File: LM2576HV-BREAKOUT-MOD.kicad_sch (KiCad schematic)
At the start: 16 parts, among them J1 Conn_01x01, J2 Conn_01x01, J3 Conn_01x01, J4 Conn_01x01, U1 LM2576HVS-ADJ

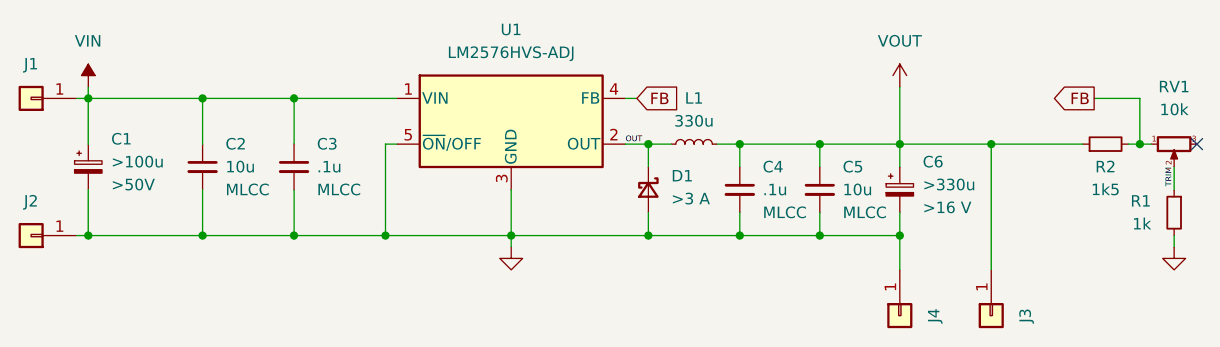
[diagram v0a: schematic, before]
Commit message: Update LM2576HV Breakout Mod to use LM2576HVS-12
- Removed unused potentiometer symbol and associated properties from schematic.
- Updated LM2576HVS-ADJ references to LM2576HVS-12 in schematic, including properties and symbols.
- Adjusted junction and wire positions for better layout.
- Removed redundant wires and no-connects to clean up the schematic.
- Updated connector positions for better alignment.
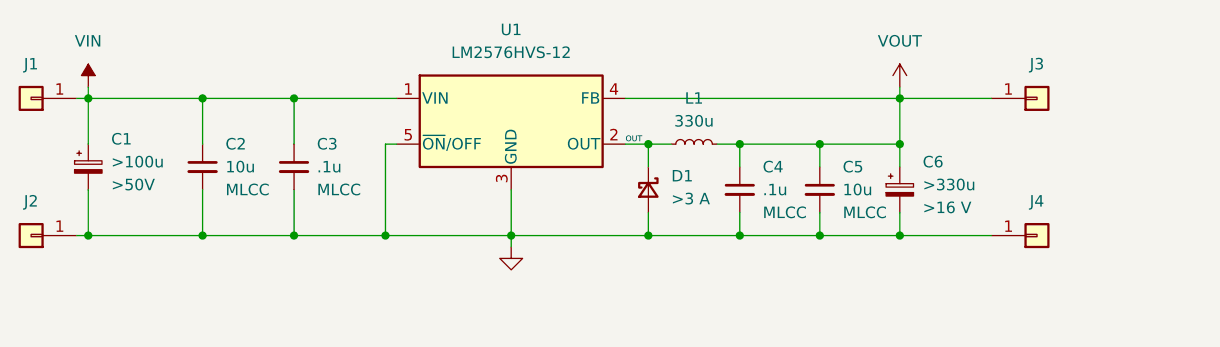
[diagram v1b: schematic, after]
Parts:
- removed R1: 1k, Resistor_SMD:R_0805_2012Metric, symbol Device:R_Small
- removed R2: 1k5, Resistor_SMD:R_0805_2012Metric, symbol Device:R_Small
- removed RV1: 10k, Potentiometer_THT:Potentiometer_Bourns_3296W_Vertical, symbol Device:R_Potentiometer_Small
- removed U1: LM2576HVS-ADJ, Package_TO_SOT_SMD:TO-263-5_TabPin3, symbol Regulator_Switching:LM2576HVS-ADJ
- added U1: LM2576HVS-12, Package_TO_SOT_SMD:TO-263-5_TabPin3, symbol Regulator_Switching:LM2576HVS-12
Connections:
- net GND: now also U1.3 (GND), U1.5 (~{ON}/OFF)
- net OUT: now also U1.2 (OUT)
- net VIN: now also U1.1 (VIN)
- net VOUT: now also U1.4 (FB)
- no-connect marks 1 -> 0
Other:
- moved on the sheet: J3, J4
